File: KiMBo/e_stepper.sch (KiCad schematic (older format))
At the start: 24 parts, among them U18 TMC2130

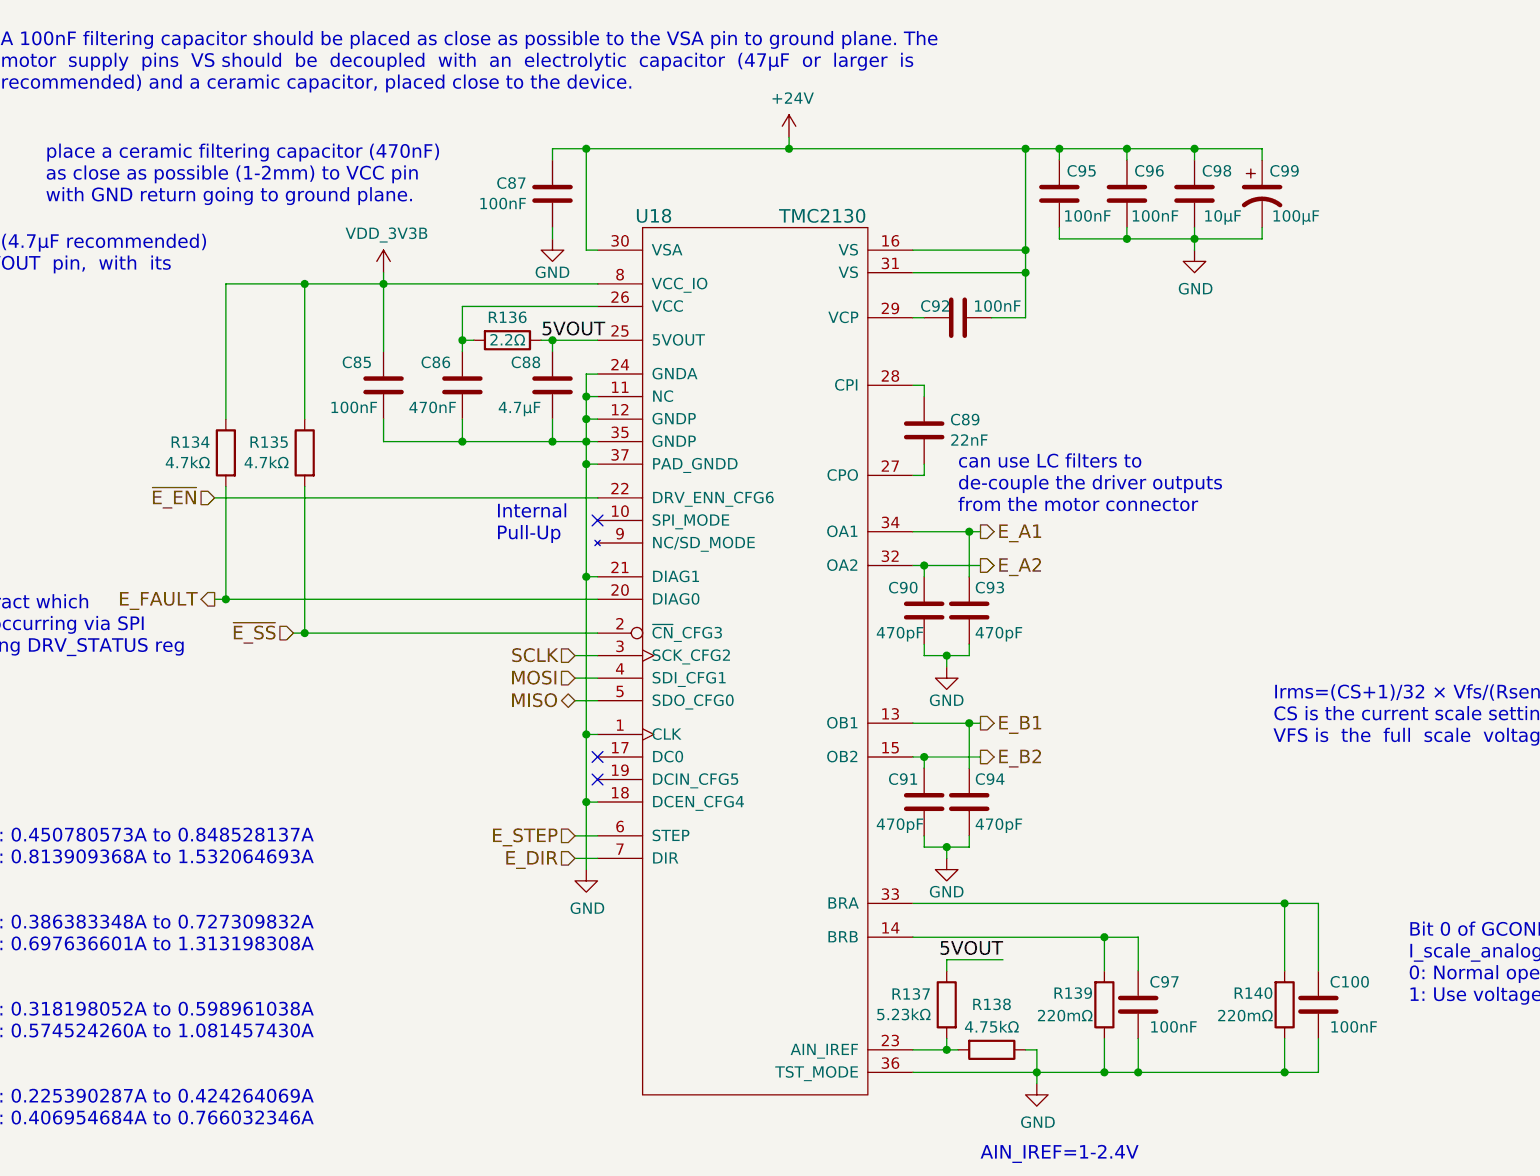
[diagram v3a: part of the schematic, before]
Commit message: Use fixed 5V LM2592HV Buck, include SPI0 header for LCD
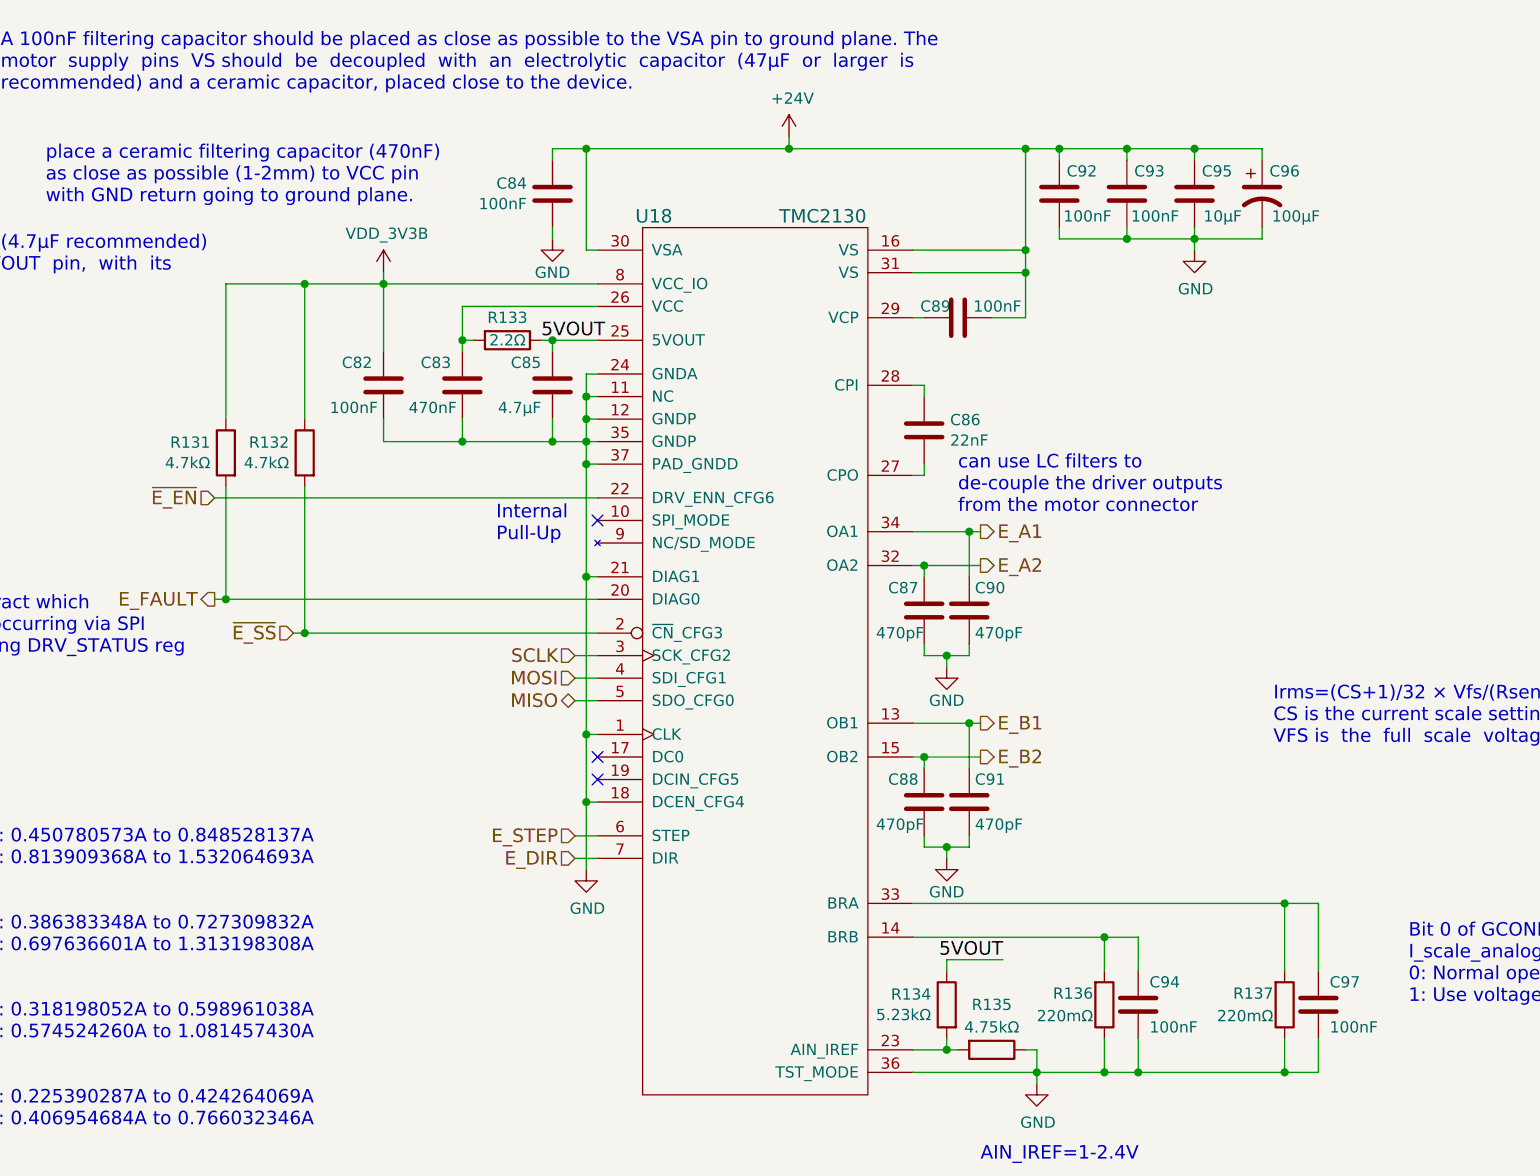
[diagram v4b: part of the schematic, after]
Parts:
- renumbered C85 to C82, C86 to C83, C87 to C84, C88 to C85, C89 to C86, C90 to C87, C91 to C88, C92 to C89, C93 to C90, C94 to C91, C95 to C92, C96 to C93, C97 to C94, C98 to C95, C99 to C96, C100 to C97, R134 to R131, R135 to R132, R136 to R133, R137 to R134, R138 to R135, R139 to R136, R140 to R137
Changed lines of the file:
@@
 MOSI
 $Comp
-L C C87
+L C C84
 U 1 1 589B8A74
 P 7300 3950
-F 0 "C87" H 7186 3904 50  0000 R CNN
+F 0 "C84" H 7186 3904 50  0000 R CNN
 F 1 "100nF" H 7186 3995 50  0000 R CNN
 F 2 "Capacitors_SMD:C_0603" H 7338 3800 50  0001 C CNN
@@
 $EndComp
 $Comp
-L C C92
+L C C89
 U 1 1 5BA7E11F
 P 9100 4500
-F 0 "C92" V 9050 4400 50  0000 C CNN
+F 0 "C89" V 9050 4400 50  0000 C CNN
 F 1 "100nF" V 9050 4675 50  0000 C CNN
 F 2 "Capacitors_SMD:C_0603" H 9138 4350 50  0001 C CNN
@@
 $EndComp
 $Comp
-L CP1 C99
+L CP1 C96
 U 1 1 5BA7E120
 P 10450 3950
-F 0 "C99" H 10550 4050 50  0000 C CNN
+F 0 "C96" H 10550 4050 50  0000 C CNN
 F 1 "100μF" H 10600 3850 50  0000 C CNN
 F 2 "Capacitors_SMD:c_elec_8x10" H 10450 3950 50  0001 C CNN
@@
 $EndComp
 $Comp
-L C C95
+L C C92
 U 1 1 589BC941
 P 9550 3950
-F 0 "C95" H 9450 4050 50  0000 C CNN
+F 0 "C92" H 9450 4050 50  0000 C CNN
 F 1 "100nF" H 9425 3850 50  0000 C CNN
 F 2 "Capacitors_SMD:C_0603" H 9588 3800 50  0001 C CNN
@@
 $EndComp
 $Comp
-L GND #PWR0199
+L GND #PWR0194
 U 1 1 589BD203
 P 7300 4150
-F 0 "#PWR0199" H 7300 3900 50  0001 C CNN
+F 0 "#PWR0194" H 7300 3900 50  0001 C CNN
 F 1 "GND" H 7300 4000 50  0000 C CNN
 F 2 "" H 7300 4150 50  0000 C CNN
@@
 $EndComp
 $Comp
-L C C96
+L C C93
 U 1 1 589BDAA2
 P 9850 3950
-F 0 "C96" H 9750 4050 50  0000 C CNN
+F 0 "C93" H 9750 4050 50  0000 C CNN
 F 1 "100nF" H 9725 3850 50  0000 C CNN
 F 2 "Capacitors_SMD:C_0603" H 9888 3800 50  0001 C CNN
@@
 $EndComp
 $Comp
-L GND #PWR0200
+L GND #PWR0195
 U 1 1 589BE47E
 P 10150 4200
-F 0 "#PWR0200" H 10150 3950 50  0001 C CNN
+F 0 "#PWR0195" H 10150 3950 50  0001 C CNN
 F 1 "GND" H 10155 4027 50  0000 C CNN
 F 2 "" H 10150 4200 50  0000 C CNN
@@
 $EndComp
 $Comp
-L +24V #PWR0201
+L +24V #PWR0196
 U 1 1 5BA7E125
 P 8350 3700
-F 0 "#PWR0201" H 8350 3550 50  0001 C CNN
+F 0 "#PWR0196" H 8350 3550 50  0001 C CNN
 F 1 "+24V" H 8365 3873 50  0000 C CNN
 F 2 "" H 8350 3700 50  0000 C CNN
@@
 $EndComp
 $Comp
-L C C89
+L C C86
 U 1 1 589C0BAD
 P 8950 5000
-F 0 "C89" H 9065 5046 50  0000 L CNN
+F 0 "C86" H 9065 5046 50  0000 L CNN
 F 1 "22nF" H 9065 4955 50  0000 L CNN
 F 2 "Capacitors_SMD:C_0402" H 8988 4850 50  0001 C CNN
@@
 $EndComp
 $Comp
-L R R140
+L R R137
 U 1 1 589C1BED
 P 10550 7550
-F 0 "R140" H 10500 7500 50  0000 R CNN
+F 0 "R137" H 10500 7500 50  0000 R CNN
 F 1 "220mΩ" H 10500 7600 50  0000 R CNN
 F 2 "" V 10480 7550 50  0001 C CNN
@@
 $EndComp
 $Comp
-L R R139
+L R R136
 U 1 1 589C1CA7
 P 9750 7550
-F 0 "R139" H 9700 7500 50  0000 R CNN
+F 0 "R136" H 9700 7500 50  0000 R CNN
 F 1 "220mΩ" H 9700 7600 50  0000 R CNN
 F 2 "" V 9680 7550 50  0001 C CNN
@@
 $EndComp
 $Comp
-L GND #PWR0202
+L GND #PWR0197
 U 1 1 5BA7E129
 P 9450 7900
-F 0 "#PWR0202" H 9450 7650 50  0001 C CNN
+F 0 "#PWR0197" H 9450 7650 50  0001 C CNN
 F 1 "GND" H 9455 7727 50  0000 C CNN
 F 2 "" H 9450 7900 50  0000 C CNN
@@
 NoConn ~ 7500 6450
 $Comp
-L R R136
+L R R133
 U 1 1 5BA7E12B
 P 7100 4600
-F 0 "R136" V 7000 4600 50  0000 C CNN
+F 0 "R133" V 7000 4600 50  0000 C CNN
 F 1 "2.2Ω" V 7100 4600 50  0000 C CNN
 F 2 "" V 7030 4600 50  0001 C CNN
@@
 $EndComp
 $Comp
-L C C86
+L C C83
 U 1 1 589C52DF
 P 6900 4800
-F 0 "C86" H 6950 4900 50  0000 L CNN
+F 0 "C83" H 6950 4900 50  0000 L CNN
 F 1 "470nF" H 6925 4700 50  0000 L CNN
 F 2 "Capacitors_SMD:C_0603" H 6938 4650 50  0001 C CNN
@@
 NoConn ~ 7500 6550
 $Comp
-L GND #PWR0203
+L GND #PWR0198
 U 1 1 589C97FF
 P 7450 6950
-F 0 "#PWR0203" H 7450 6700 50  0001 C CNN
+F 0 "#PWR0198" H 7450 6700 50  0001 C CNN
 F 1 "GND" H 7455 6777 50  0000 C CNN
 F 2 "" H 7450 6950 50  0000 C CNN
@@
 $EndComp
 $Comp
-L C C97
+L C C94
 U 1 1 5BA7E12E
 P 9900 7550
-F 0 "C97" H 9950 7650 50  0000 L CNN
+F 0 "C94" H 9950 7650 50  0000 L CNN
 F 1 "100nF" H 9950 7450 50  0000 L CNN
 F 2 "Capacitors_SMD:C_0603" H 9938 7400 50  0001 C CNN
@@
 E_FAULT
 $Comp
-L R R134
+L R R131
 U 1 1 589D21BC
 P 5850 5100
-F 0 "R134" H 5919 5146 50  0000 L CNN
+F 0 "R131" H 5919 5146 50  0000 L CNN
 F 1 "4.7kΩ" H 5919 5055 50  0000 L CNN
 F 2 "" V 5780 5100 50  0001 C CNN
@@
 Internal\nPull-Up
 $Comp
-L C C88
+L C C85
 U 1 1 5BA7E12A
 P 7300 4800
-F 0 "C88" H 7350 4900 50  0000 L CNN
+F 0 "C85" H 7350 4900 50  0000 L CNN
 F 1 "4.7μF" H 7350 4700 50  0000 L CNN
 F 2 "Capacitors_SMD:C_0402" H 7338 4650 50  0001 C CNN
@@
 5VOUT
 $Comp
-L R R137
+L R R134
 U 1 1 589E13FD
 P 9050 7550
-F 0 "R137" H 9119 7596 50  0000 L CNN
+F 0 "R134" H 9119 7596 50  0000 L CNN
 F 1 "5.23kΩ" H 9119 7505 50  0000 L CNN
 F 2 "" V 8980 7550 50  0001 C CNN
@@
 5VOUT
 $Comp
-L R R138
+L R R135
 U 1 1 589E24D4
 P 9250 7750
-F 0 "R138" V 9050 7750 50  0000 C CNN
+F 0 "R135" V 9050 7750 50  0000 C CNN
 F 1 "4.75kΩ" V 9150 7750 50  0000 C CNN
 F 2 "" V 9180 7750 50  0001 C CNN
@@
 AIN_IREF=1-2.4V
 $Comp
-L R R135
+L R R132
 U 1 1 5BA7E132
 P 6200 5100
-F 0 "R135" H 6269 5146 50  0000 L CNN
+F 0 "R132" H 6269 5146 50  0000 L CNN
 F 1 "4.7kΩ" H 6269 5055 50  0000 L CNN
 F 2 "" V 6130 5100 50  0001 C CNN
@@
 $EndComp
 $Comp
-L C C100
+L C C97
 U 1 1 5BA7E133
 P 10700 7550
-F 0 "C100" H 10750 7650 50  0000 L CNN
+F 0 "C97" H 10750 7650 50  0000 L CNN
 F 1 "100nF" H 10750 7450 50  0000 L CNN
 F 2 "Capacitors_SMD:C_0603" H 10738 7400 50  0001 C CNN
@@
 Choose  sense  resistors  in  a  way,  that  normal \nIRUN is 16 to 31 for best microstep performance.
 $Comp
-L C C90
+L C C87
 U 1 1 5BA7E134
 P 8950 5800
-F 0 "C90" H 8975 5900 50  0000 L CNN
+F 0 "C87" H 8975 5900 50  0000 L CNN
 F 1 "470pF" H 8950 5700 50  0000 L CNN
 F 2 "Capacitors_SMD:C_0603" H 8988 5650 50  0001 C CNN
@@
 $EndComp
 $Comp
-L GND #PWR0204
+L GND #PWR0199
 U 1 1 58B19D33
 P 9050 6050
-F 0 "#PWR0204" H 9050 5800 50  0001 C CNN
+F 0 "#PWR0199" H 9050 5800 50  0001 C CNN
 F 1 "GND" H 9050 5900 50  0000 C CNN
 F 2 "" H 9050 6050 50  0000 C CNN
@@
 $EndComp
 $Comp
-L C C93
+L C C90
 U 1 1 58B1B794
 P 9150 5800
-F 0 "C93" H 9175 5900 50  0000 L CNN
+F 0 "C90" H 9175 5900 50  0000 L CNN
 F 1 "470pF" H 9175 5700 50  0000 L CNN
 F 2 "Capacitors_SMD:C_0603" H 9188 5650 50  0001 C CNN
@@
 $EndComp
 $Comp
-L C C91
+L C C88
 U 1 1 58B1C6FD
 P 8950 6650
-F 0 "C91" H 8975 6750 50  0000 L CNN
+F 0 "C88" H 8975 6750 50  0000 L CNN
 F 1 "470pF" H 8950 6550 50  0000 L CNN
 F 2 "Capacitors_SMD:C_0603" H 8988 6500 50  0001 C CNN
@@
 $EndComp
 $Comp
-L GND #PWR0205
+L GND #PWR0200
 U 1 1 58B1C704
 P 9050 6900
-F 0 "#PWR0205" H 9050 6650 50  0001 C CNN
+F 0 "#PWR0200" H 9050 6650 50  0001 C CNN
 F 1 "GND" H 9050 6750 50  0000 C CNN
 F 2 "" H 9050 6900 50  0000 C CNN
@@
 $EndComp
 $Comp
-L C C94
+L C C91
 U 1 1 58B1C710
 P 9150 6650
-F 0 "C94" H 9175 6750 50  0000 L CNN
+F 0 "C91" H 9175 6750 50  0000 L CNN
 F 1 "470pF" H 9175 6550 50  0000 L CNN
 F 2 "Capacitors_SMD:C_0603" H 9188 6500 50  0001 C CNN
@@
 $EndComp
 $Comp
-L C C98
+L C C95
 U 1 1 58B40194
 P 10150 3950
-F 0 "C98" H 10050 4050 50  0000 C CNN
+F 0 "C95" H 10050 4050 50  0000 C CNN
 F 1 "10μF" H 10025 3850 50  0000 C CNN
 F 2 "Capacitors_SMD:C_0805" H 10188 3800 50  0001 C CNN
@@
 Can extract which\nfault is occurring via SPI\nby reading DRV_STATUS reg
 $Comp
-L VDD_3V3B #PWR0206
+L VDD_3V3B #PWR0201
 U 1 1 5A2FD350
 P 6550 4300
-F 0 "#PWR0206" H 6550 4150 50  0001 C CNN
+F 0 "#PWR0201" H 6550 4150 50  0001 C CNN
 F 1 "VDD_3V3B" H 6565 4473 50  0000 C CNN
 F 2 "" H 6550 4300 50  0000 C CNN
@@
 $EndComp
 $Comp
-L C C85
+L C C82
 U 1 1 5A896678
 P 6550 4800
-F 0 "C85" H 6600 4900 50  0000 L CNN
+F 0 "C82" H 6600 4900 50  0000 L CNN
 F 1 "100nF" H 6575 4700 50  0000 L CNN
 F 2 "Capacitors_SMD:C_0603" H 6588 4650 50  0001 C CNN

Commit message: Assocate more footprints
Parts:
- C85, C86: footprint Capacitors_SMD:C_0402 -> Capacitors_SMD:C_0603
- R131, R132, R133, R134, R135: footprint (none) -> Resistors_SMD:R_0603
- U18: footprint (none) -> KiMBo:QFN36_5X6
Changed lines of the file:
@@
 F 0 "C86" H 9065 5046 50  0000 L CNN
 F 1 "22nF" H 9065 4955 50  0000 L CNN
-F 2 "Capacitors_SMD:C_0402" H 8988 4850 50  0001 C CNN
+F 2 "Capacitors_SMD:C_0603" H 8988 4850 50  0001 C CNN
 F 3 "" H 8950 5000 50  0000 C CNN
 	1    8950 5000
@@
 F 0 "R133" V 7000 4600 50  0000 C CNN
 F 1 "2.2Ω" V 7100 4600 50  0000 C CNN
-F 2 "" V 7030 4600 50  0001 C CNN
+F 2 "Resistors_SMD:R_0603" V 7030 4600 50  0001 C CNN
 F 3 "" H 7100 4600 50  0000 C CNN
 	1    7100 4600
@@
 F 0 "R131" H 5919 5146 50  0000 L CNN
 F 1 "4.7kΩ" H 5919 5055 50  0000 L CNN
-F 2 "" V 5780 5100 50  0001 C CNN
+F 2 "Resistors_SMD:R_0603" V 5780 5100 50  0001 C CNN
 F 3 "" H 5850 5100 50  0000 C CNN
 	1    5850 5100
@@
 F 0 "C85" H 7350 4900 50  0000 L CNN
 F 1 "4.7μF" H 7350 4700 50  0000 L CNN
-F 2 "Capacitors_SMD:C_0402" H 7338 4650 50  0001 C CNN
+F 2 "Capacitors_SMD:C_0603" H 7338 4650 50  0001 C CNN
 F 3 "" H 7300 4800 50  0000 C CNN
 	1    7300 4800
@@
 F 0 "R134" H 9119 7596 50  0000 L CNN
 F 1 "5.23kΩ" H 9119 7505 50  0000 L CNN
-F 2 "" V 8980 7550 50  0001 C CNN
+F 2 "Resistors_SMD:R_0603" V 8980 7550 50  0001 C CNN
 F 3 "" H 9050 7550 50  0000 C CNN
 	1    9050 7550
@@
 F 0 "R135" V 9050 7750 50  0000 C CNN
 F 1 "4.75kΩ" V 9150 7750 50  0000 C CNN
-F 2 "" V 9180 7750 50  0001 C CNN
+F 2 "Resistors_SMD:R_0603" V 9180 7750 50  0001 C CNN
 F 3 "" H 9250 7750 50  0000 C CNN
 	1    9250 7750
@@
 F 0 "R132" H 6269 5146 50  0000 L CNN
 F 1 "4.7kΩ" H 6269 5055 50  0000 L CNN
-F 2 "" V 6130 5100 50  0001 C CNN
+F 2 "Resistors_SMD:R_0603" V 6130 5100 50  0001 C CNN
 F 3 "" H 6200 5100 50  0000 C CNN
 	1    6200 5100
@@
 F 0 "U18" H 7750 7050 60  0000 C CNN
 F 1 "TMC2130" H 8500 7050 60  0000 C CNN
-F 2 "" H 8200 5850 60  0001 C CNN
+F 2 "KiMBo:QFN36_5X6" H 8200 5850 60  0001 C CNN
 F 3 "" H 8200 5850 60  0000 C CNN
 	1    8200 5550

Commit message: More footprint association
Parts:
- R136, R137: footprint (none) -> Resistors_SMD:R_0805
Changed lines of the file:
@@
 $EndComp
 $Comp
-L GND #PWR0194
+L GND #PWR0195
 U 1 1 589BD203
 P 7300 4150
-F 0 "#PWR0194" H 7300 3900 50  0001 C CNN
+F 0 "#PWR0195" H 7300 3900 50  0001 C CNN
 F 1 "GND" H 7300 4000 50  0000 C CNN
 F 2 "" H 7300 4150 50  0000 C CNN
@@
 $EndComp
 $Comp
-L GND #PWR0195
+L GND #PWR0196
 U 1 1 589BE47E
 P 10150 4200
-F 0 "#PWR0195" H 10150 3950 50  0001 C CNN
+F 0 "#PWR0196" H 10150 3950 50  0001 C CNN
 F 1 "GND" H 10155 4027 50  0000 C CNN
 F 2 "" H 10150 4200 50  0000 C CNN
@@
 $EndComp
 $Comp
-L +24V #PWR0196
+L +24V #PWR0197
 U 1 1 5BA7E125
 P 8350 3700
-F 0 "#PWR0196" H 8350 3550 50  0001 C CNN
+F 0 "#PWR0197" H 8350 3550 50  0001 C CNN
 F 1 "+24V" H 8365 3873 50  0000 C CNN
 F 2 "" H 8350 3700 50  0000 C CNN
@@
 F 0 "R137" H 10500 7500 50  0000 R CNN
 F 1 "220mΩ" H 10500 7600 50  0000 R CNN
-F 2 "" V 10480 7550 50  0001 C CNN
+F 2 "Resistors_SMD:R_0805" V 10480 7550 50  0001 C CNN
 F 3 "" H 10550 7550 50  0000 C CNN
 	1    10550 7550
@@
 F 0 "R136" H 9700 7500 50  0000 R CNN
 F 1 "220mΩ" H 9700 7600 50  0000 R CNN
-F 2 "" V 9680 7550 50  0001 C CNN
+F 2 "Resistors_SMD:R_0805" V 9680 7550 50  0001 C CNN
 F 3 "" H 9750 7550 50  0000 C CNN
 	1    9750 7550
@@
 $EndComp
 $Comp
-L GND #PWR0197
+L GND #PWR0198
 U 1 1 5BA7E129
 P 9450 7900
-F 0 "#PWR0197" H 9450 7650 50  0001 C CNN
+F 0 "#PWR0198" H 9450 7650 50  0001 C CNN
 F 1 "GND" H 9455 7727 50  0000 C CNN
 F 2 "" H 9450 7900 50  0000 C CNN
@@
 NoConn ~ 7500 6550
 $Comp
-L GND #PWR0198
+L GND #PWR0199
 U 1 1 589C97FF
 P 7450 6950
-F 0 "#PWR0198" H 7450 6700 50  0001 C CNN
+F 0 "#PWR0199" H 7450 6700 50  0001 C CNN
 F 1 "GND" H 7455 6777 50  0000 C CNN
 F 2 "" H 7450 6950 50  0000 C CNN
@@
 $EndComp
 $Comp
-L GND #PWR0199
+L GND #PWR0200
 U 1 1 58B19D33
 P 9050 6050
-F 0 "#PWR0199" H 9050 5800 50  0001 C CNN
+F 0 "#PWR0200" H 9050 5800 50  0001 C CNN
 F 1 "GND" H 9050 5900 50  0000 C CNN
 F 2 "" H 9050 6050 50  0000 C CNN
@@
 $EndComp
 $Comp
-L GND #PWR0200
+L GND #PWR0201
 U 1 1 58B1C704
 P 9050 6900
-F 0 "#PWR0200" H 9050 6650 50  0001 C CNN
+F 0 "#PWR0201" H 9050 6650 50  0001 C CNN
 F 1 "GND" H 9050 6750 50  0000 C CNN
 F 2 "" H 9050 6900 50  0000 C CNN
@@
 Can extract which\nfault is occurring via SPI\nby reading DRV_STATUS reg
 $Comp
-L VDD_3V3B #PWR0201
+L VDD_3V3B #PWR0202
 U 1 1 5A2FD350
 P 6550 4300
-F 0 "#PWR0201" H 6550 4150 50  0001 C CNN
+F 0 "#PWR0202" H 6550 4150 50  0001 C CNN
 F 1 "VDD_3V3B" H 6565 4473 50  0000 C CNN
 F 2 "" H 6550 4300 50  0000 C CNN
